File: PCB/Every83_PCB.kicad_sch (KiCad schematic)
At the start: 31 parts, among them J1 781710004, J3 SM03B-SRSS-TB, J4 SM03B-SRSS-TB, Q3 DMG2305, SW101 KMR2, SW102 KMR2, U2 AP2112(3.3V), U3 MCP73831T-2ACI/OT, X3 JSTPH

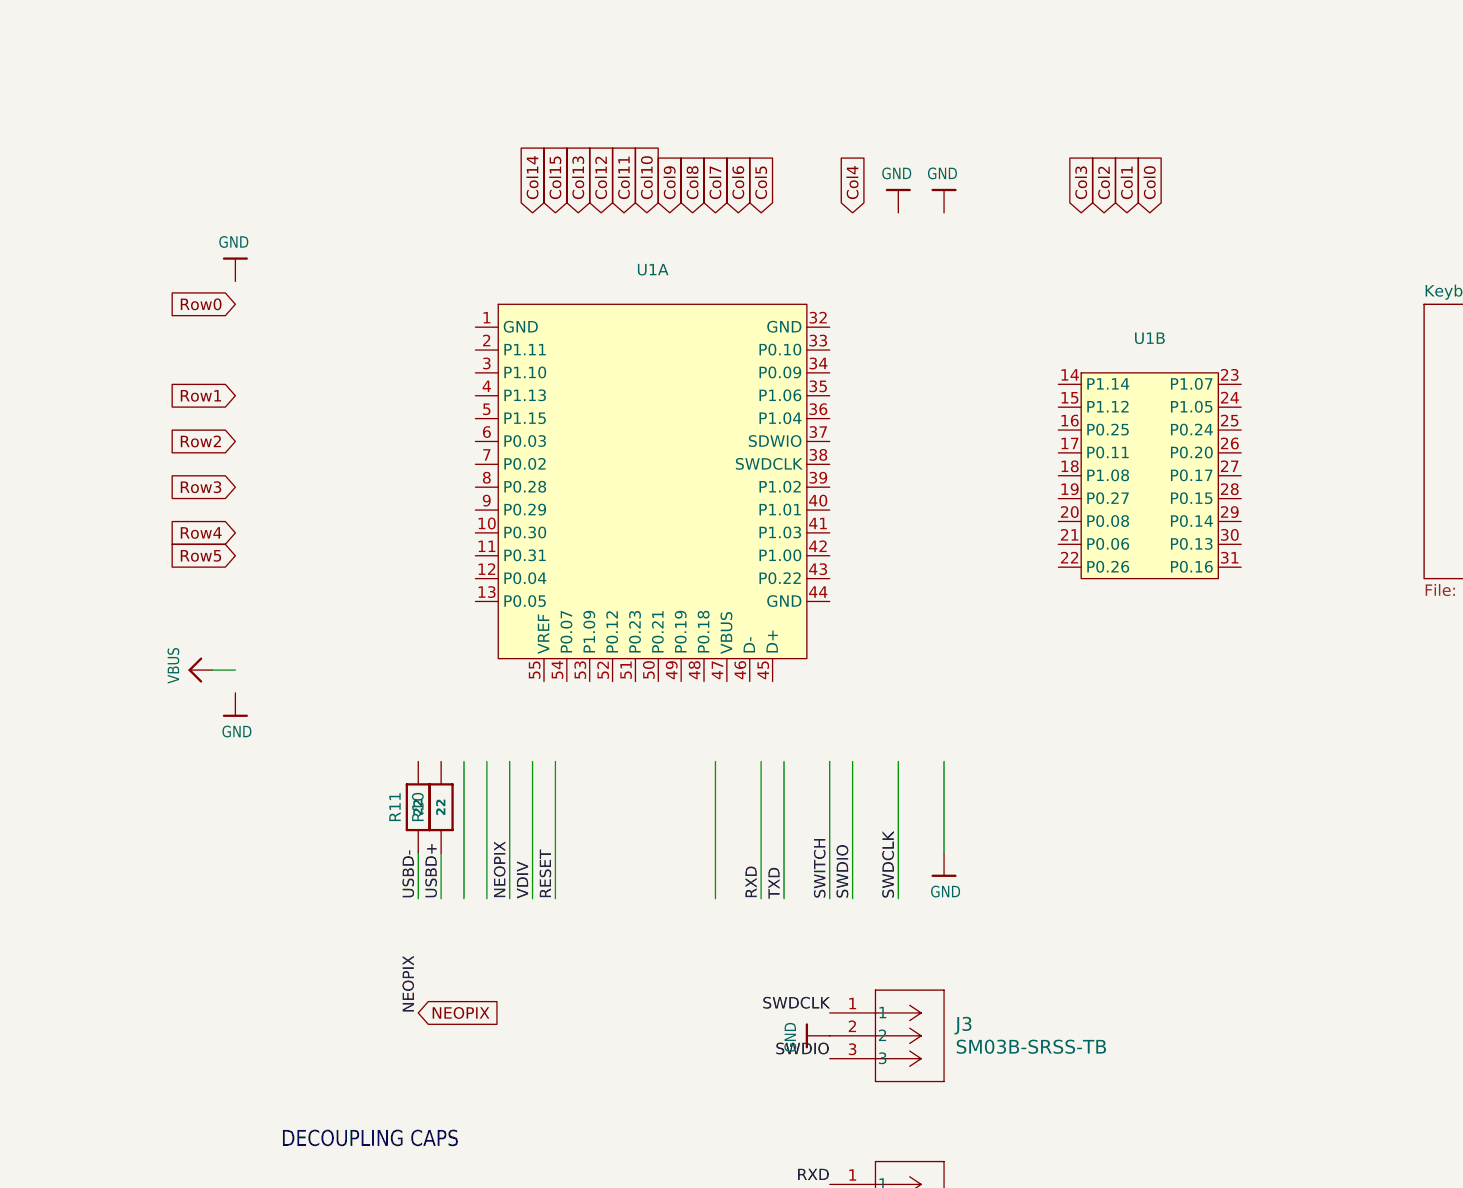
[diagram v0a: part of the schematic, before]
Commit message: Update the microcontroller footprint
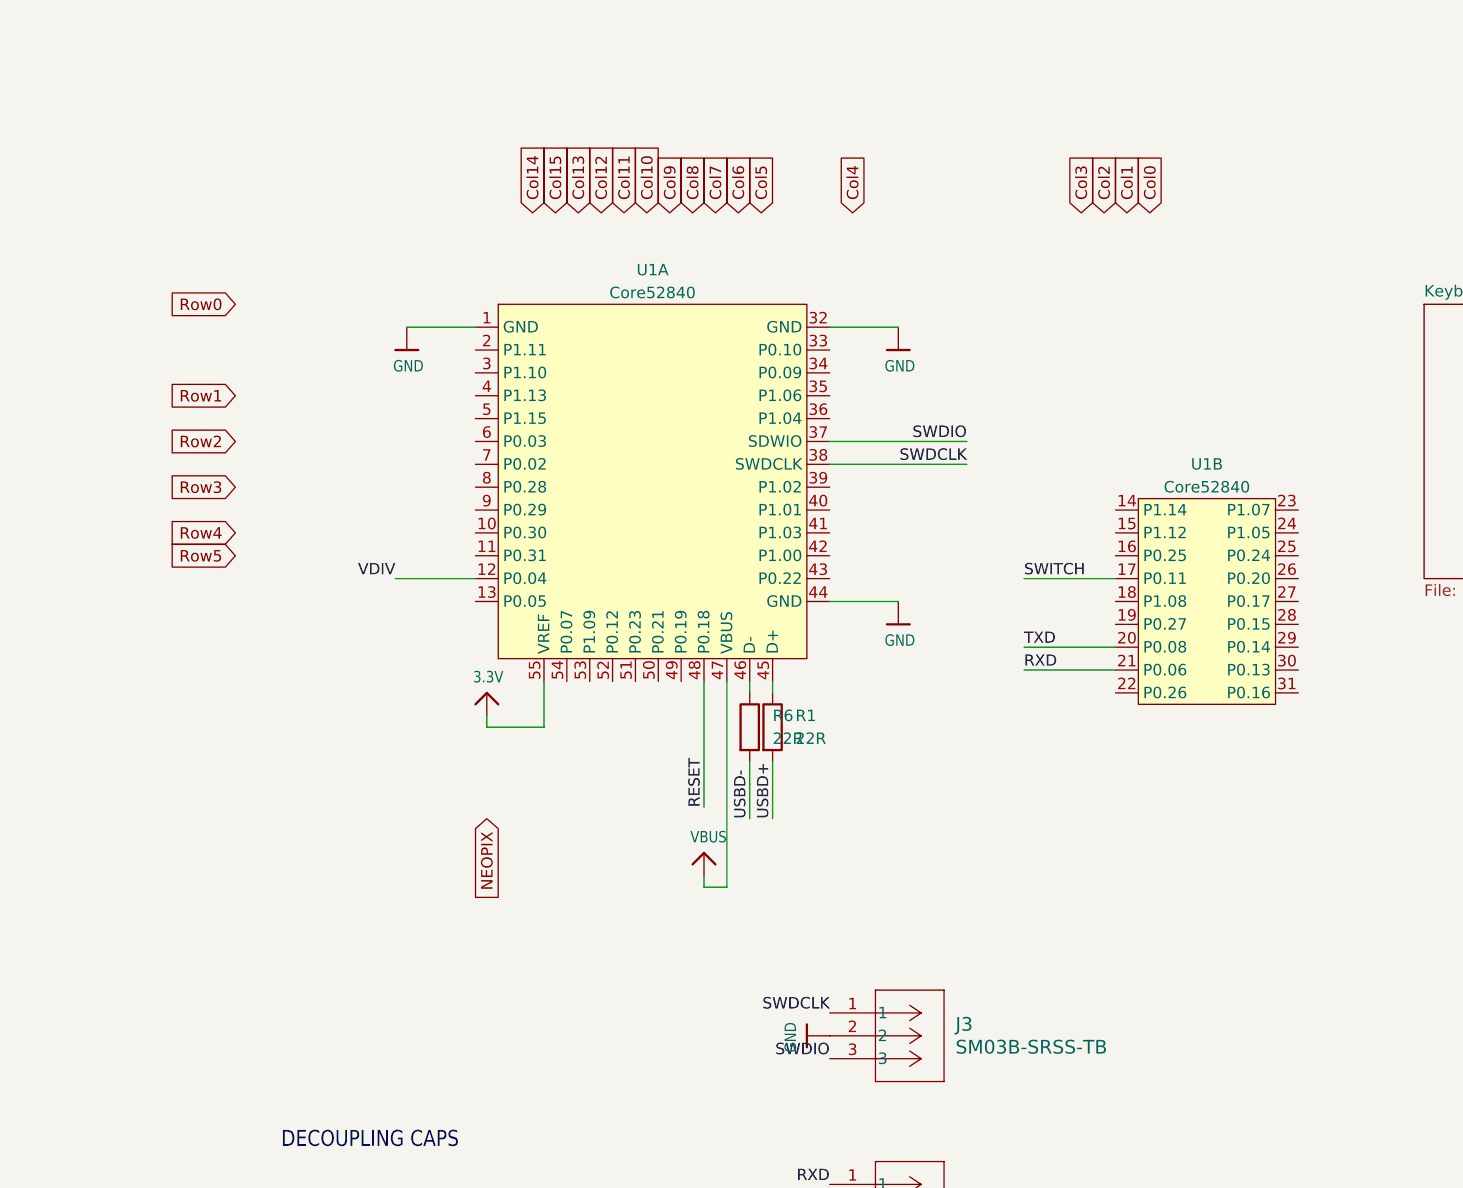
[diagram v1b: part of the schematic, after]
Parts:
- removed R10, R11: 22, Adafruit nRF52840 Bluefruit Feather Express Rev D:0603-NO, symbol Adafruit nRF52840 Bluefruit Feather Express Rev D-eagle-import:RESISTOR_0603_NO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
- added R1, R6: 22R, Resistor_SMD:R_0603_1608Metric, symbol Device:R
- U1: value ~ -> Core52840; footprint (none) -> footprints:Core52840
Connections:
- net 3.3V: now also U1.55 (VREF)
- net GND: now also U1.1 (GND), U1.32 (GND), U1.44 (GND)
- net RESET: now also U1.48 (P0.18)
- net RXD: now also U1.21 (P0.06)
- net SWDCLK: now also U1.38 (SWDCLK)
- net SWDIO: now also U1.37 (SDWIO)
- net SWITCH: now also U1.17 (P0.11)
- net TXD: now also U1.20 (P0.08)
- net USBD+: now also R1.2
- net USBD-: now also R6.2
- net VBUS: now also U1.47 (VBUS)
- net VDIV: now also U1.12 (P0.04)
- net at U1.45 (D+): now also R1.1
- net at U1.46 (D-): now also R6.1
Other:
- moved on the sheet: U1B

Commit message: More work done
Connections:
- net Col0: now also U1.2 (P1.11)
- net Col1: now also U1.3 (P1.10)
- net Col10: now also U1.13 (P0.05)
- net Col2: now also U1.4 (P1.13)
- net Col3: now also U1.5 (P1.15)
- net Col4: now also U1.6 (P0.03)
- net Col5: now also U1.7 (P0.02)
- net Col6: now also U1.8 (P0.28)
- net Col7: now also U1.9 (P0.29)
- net Col8: now also U1.10 (P0.30)
- net Col9: now also U1.11 (P0.31)
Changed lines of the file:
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@@
 	(wire
 		(pts
-			(xy 120.65 81.28) (xy 128.27 81.28)
+			(xy 116.84 81.28) (xy 128.27 81.28)
 		)
 		(stroke
@@
 	(global_label "Col10"
 		(shape input)
-		(at 147.32 68.58 90)
+		(at 128.27 111.76 180)
 		(fields_autoplaced yes)
 		(effects
@@
 				(size 1.27 1.27)
 			)
-			(justify left)
+			(justify right)
 		)
 		(property "Intersheetrefs" "${INTERSHEET_REFS}"
-			(at 147.32 60.171 90)
+			(at 119.7816 111.76 0)
 			(effects
 				(font
 					(size 1.27 1.27)
 				)
-				(justify left)
+				(justify right)
 				(hide yes)
 			)
@@
 	(global_label "Col8"
 		(shape input)
-		(at 152.4 68.58 90)
+		(at 128.27 104.14 180)
 		(fields_autoplaced yes)
 		(effects
@@
 				(size 1.27 1.27)
 			)
-			(justify left)
+			(justify right)
 		)
 		(property "Intersheetrefs" "${INTERSHEET_REFS}"
-			(at 152.4 61.3011 90)
+			(at 120.9911 104.14 0)
 			(effects
 				(font
 					(size 1.27 1.27)
 				)
-				(justify left)
+				(justify right)
 				(hide yes)
 			)
@@
 	(global_label "Col5"
 		(shape input)
-		(at 160.02 68.58 90)
+		(at 128.27 96.52 180)
 		(fields_autoplaced yes)
 		(effects
@@
 				(size 1.27 1.27)
 			)
-			(justify left)
+			(justify right)
 		)
 		(property "Intersheetrefs" "${INTERSHEET_REFS}"
-			(at 160.02 61.3011 90)
+			(at 120.9911 96.52 0)
 			(effects
 				(font
 					(size 1.27 1.27)
 				)
-				(justify left)
+				(justify right)
 				(hide yes)
 			)
@@
 	(global_label "Col7"
 		(shape input)
-		(at 154.94 68.58 90)
+		(at 128.27 101.6 180)
 		(fields_autoplaced yes)
 		(effects
@@
 				(size 1.27 1.27)
 			)
-			(justify left)
+			(justify right)
 		)
 		(property "Intersheetrefs" "${INTERSHEET_REFS}"
-			(at 154.94 61.3011 90)
+			(at 120.9911 101.6 0)
 			(effects
 				(font
 					(size 1.27 1.27)
 				)
-				(justify left)
+				(justify right)
 				(hide yes)
 			)
@@
 	(global_label "Col9"
 		(shape input)
-		(at 149.86 68.58 90)
+		(at 128.27 106.68 180)
 		(fields_autoplaced yes)
 		(effects
@@
 				(size 1.27 1.27)
 			)
-			(justify left)
+			(justify right)
 		)
 		(property "Intersheetrefs" "${INTERSHEET_REFS}"
-			(at 149.86 61.3805 90)
+			(at 120.9911 106.68 0)
 			(effects
 				(font
 					(size 1.27 1.27)
 				)
-				(justify left)
+				(justify right)
 				(hide yes)
 			)
@@
 	(global_label "Col6"
 		(shape input)
-		(at 157.48 68.58 90)
+		(at 128.27 99.06 180)
 		(fields_autoplaced yes)
 		(effects
@@
 				(size 1.27 1.27)
 			)
-			(justify left)
+			(justify right)
 		)
 		(property "Intersheetrefs" "${INTERSHEET_REFS}"
-			(at 157.48 61.3011 90)
+			(at 120.9911 99.06 0)
 			(effects
 				(font
 					(size 1.27 1.27)
 				)
-				(justify left)
+				(justify right)
 				(hide yes)
 			)
@@
 	(global_label "Col2"
 		(shape input)
-		(at 198.12 68.58 90)
+		(at 128.27 88.9 180)
 		(fields_autoplaced yes)
 		(effects
@@
 				(size 1.27 1.27)
 			)
-			(justify left)
+			(justify right)
 		)
 		(property "Intersheetrefs" "${INTERSHEET_REFS}"
-			(at 198.12 61.3011 90)
+			(at 120.9911 88.9 0)
 			(effects
 				(font
 					(size 1.27 1.27)
 				)
-				(justify left)
+				(justify right)
 				(hide yes)
 			)
@@
 	(global_label "Col3"
 		(shape input)
-		(at 195.58 68.58 90)
+		(at 128.27 91.44 180)
 		(fields_autoplaced yes)
 		(effects
@@
 				(size 1.27 1.27)
 			)
-			(justify left)
+			(justify right)
 		)
 		(property "Intersheetrefs" "${INTERSHEET_REFS}"
-			(at 195.58 61.3011 90)
+			(at 120.9911 91.44 0)
 			(effects
 				(font
 					(size 1.27 1.27)
 				)
-				(justify left)
+				(justify right)
 				(hide yes)
 			)
@@
 	(global_label "Col1"
 		(shape input)
-		(at 200.66 68.58 90)
+		(at 128.27 86.36 180)
 		(fields_autoplaced yes)
 		(effects
@@
 				(size 1.27 1.27)
 			)
-			(justify left)
+			(justify right)
 		)
 		(property "Intersheetrefs" "${INTERSHEET_REFS}"
-			(at 200.66 61.3011 90)
+			(at 120.9911 86.36 0)
 			(effects
 				(font
 					(size 1.27 1.27)
 				)
-				(justify left)
+				(justify right)
 				(hide yes)
 			)
@@
 	(global_label "Col0"
 		(shape input)
-		(at 203.2 68.58 90)
+		(at 128.27 83.82 180)
 		(fields_autoplaced yes)
 		(effects
@@
 				(size 1.27 1.27)
 			)
-			(justify left)
+			(justify right)
 		)
 		(property "Intersheetrefs" "${INTERSHEET_REFS}"
-			(at 203.2 61.3011 90)
+			(at 120.9911 83.82 0)
 			(effects
 				(font
 					(size 1.27 1.27)
 				)
-				(justify left)
+				(justify right)
 				(hide yes)
 			)
@@
 	(global_label "Col4"
 		(shape input)
-		(at 170.18 68.58 90)
+		(at 128.27 93.98 180)
 		(fields_autoplaced yes)
 		(effects
@@
 				(size 1.27 1.27)
 			)
-			(justify left)
+			(justify right)
 		)
 		(property "Intersheetrefs" "${INTERSHEET_REFS}"
-			(at 170.18 61.3011 90)
+			(at 120.9911 93.98 0)
 			(effects
 				(font
 					(size 1.27 1.27)
 				)
-				(justify left)
+				(justify right)
 				(hide yes)
 			)
@@
 	(symbol
 		(lib_id "Adafruit nRF52840 Bluefruit Feather Express Rev D-eagle-import:GND")
-		(at 120.65 83.82 0)
+		(at 116.84 83.82 0)
 		(unit 1)
 		(exclude_from_sim no)
@@
 		(dnp no)
 		(property "Reference" "#U$048"
-			(at 120.65 83.82 0)
+			(at 116.84 83.82 0)
 			(effects
 				(font
@@
 		)
 		(property "Value" "GND"
-			(at 119.126 86.36 0)
+			(at 115.316 86.36 0)
 			(effects
 				(font
@@
 		)
 		(property "Footprint" ""
-			(at 120.65 83.82 0)
+			(at 116.84 83.82 0)
 			(effects
 				(font
@@
 		)
 		(property "Datasheet" ""
-			(at 120.65 83.82 0)
+			(at 116.84 83.82 0)
 			(effects
 				(font
@@
 		)
 		(property "Description" ""
-			(at 120.65 83.82 0)
+			(at 116.84 83.82 0)
 			(effects
 				(font

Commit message: Just need to run DRC now
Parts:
- removed D102: RED, Adafruit nRF52840 Bluefruit Feather Express Rev D:CHIPLED_0805_NOOUTLINE, symbol Adafruit nRF52840 Bluefruit Feather Express Rev D-eagle-import:LED0805_NOOUTLINE
- removed D104: BLUE, Adafruit nRF52840 Bluefruit Feather Express Rev D:CHIPLED_0805_NOOUTLINE, symbol Adafruit nRF52840 Bluefruit Feather Express Rev D-eagle-import:LED0805_NOOUTLINE
- added D84, D85: LED, LED_SMD:LED_0805_2012Metric, symbol Device:LED
- R2, R3, R5: footprint Adafruit nRF52840 Bluefruit Feather Express Rev D:0603-NO -> Resistor_SMD:R_0603_1608Metric
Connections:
- net Col11: now also U1.54 (P0.07)
- net Col12: now also U1.53 (P1.09)
- net Col13: now also U1.52 (P0.12)
- net Col14: now also U1.51 (P0.23)
- net Col15: now also U1.50 (P0.21)
- net GND: now also R2.2
- net LED1: now also U1.43 (P0.22), D84.2 (A); no longer R2.1
- net LED2: now also U1.42 (P1.00), D85.2 (A)
- net NEOPIX: now also U1.49 (P0.19)
- net Row0: now also U1.26 (P0.20)
- net Row1: now also U1.27 (P0.17)
- net Row2: now also U1.28 (P0.15)
- net Row3: now also U1.29 (P0.14)
- net Row4: now also U1.30 (P0.13)
- net Row5: now also U1.31 (P0.16)
- net at R5.1: now also D85.1 (K)
- new net: D84.1 (K), R2.1
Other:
- moved on the sheet: R2

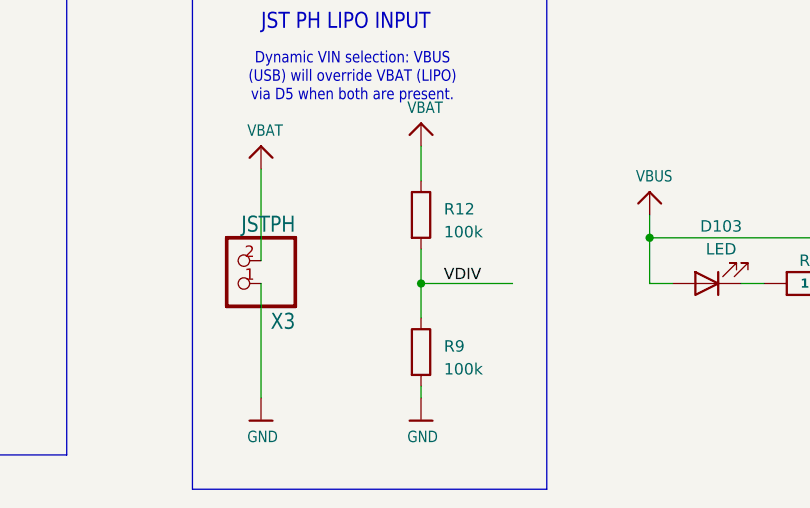
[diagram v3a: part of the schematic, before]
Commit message: change battery connector
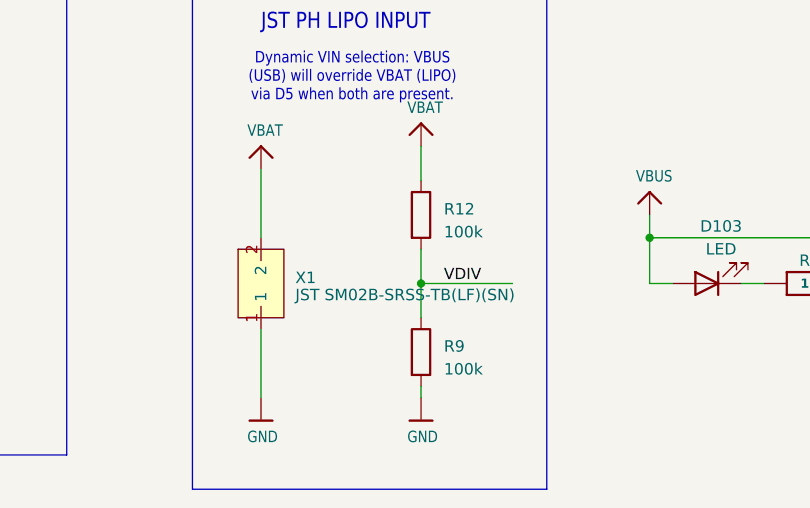
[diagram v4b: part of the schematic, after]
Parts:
- removed X3: JSTPH, Adafruit nRF52840 Bluefruit Feather Express Rev D:JSTPH2, symbol Adafruit nRF52840 Bluefruit Feather Express Rev D-eagle-import:CON_JST_PH_2PIN
- added X1: JST SM02B-SRSS-TB(LF)(SN), Connector_JST:JST_SH_SM02B-SRSS-TB_1x02-1MP_P1.00mm_Horizontal, symbol JohnDeere:SM02B-SRSS-TB
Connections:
- net GND: now also X1.1
- net VBAT: now also X1.2
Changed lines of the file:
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@@
 	(wire
 		(pts
-			(xy 177.8 233.68) (xy 177.8 243.84)
-		)
-		(stroke
-			(width 0.1524)
-			(type solid)
-		)
-	)
-	(wire
-		(pts
 			(xy 121.92 193.04) (xy 121.92 195.58)
 		)
@@
 	(wire
 		(pts
-			(xy 177.8 259.08) (xy 177.8 246.38)
-		)
-		(stroke
-			(width 0.1524)
-			(type solid)
-		)
-	)
-	(wire
-		(pts
 			(xy 153.67 143.51) (xy 156.21 143.51)
 		)
@@
 	(wire
 		(pts
+			(xy 177.8 233.68) (xy 177.8 241.3)
+		)
+		(stroke
+			(width 0)
+			(type default)
+		)
+	)
+	(wire
+		(pts
 			(xy 88.9 254) (xy 88.9 251.46)
 		)
@@
 	(wire
 		(pts
+			(xy 177.8 251.46) (xy 177.8 259.08)
+		)
+		(stroke
+			(width 0)
+			(type default)
+		)
+	)
+	(wire
+		(pts
 			(xy 99.06 243.84) (xy 99.06 238.76)
 		)
@@
 	)
 	(symbol
-		(lib_id "Adafruit nRF52840 Bluefruit Feather Express Rev D-eagle-import:CON_JST_PH_2PIN")
-		(at 175.26 243.84 180)
-		(unit 1)
-		(exclude_from_sim no)
-		(in_bom yes)
-		(on_board yes)
-		(dnp no)
-		(property "Reference" "X3"
-			(at 181.61 249.555 0)
-			(effects
-				(font
-					(size 1.778 1.5113)
-				)
-				(justify left bottom)
-			)
-		)
-		(property "Value" "JSTPH"
-			(at 181.61 238.76 0)
-			(effects
-				(font
-					(size 1.778 1.5113)
-				)
-				(justify left bottom)
-			)
-		)
-		(property "Footprint" "Adafruit nRF52840 Bluefruit Feather Express Rev D:JSTPH2"
-			(at 175.26 243.84 0)
-			(effects
-				(font
-					(size 1.27 1.27)
-				)
-				(hide yes)
-			)
-		)
-		(property "Datasheet" ""
-			(at 175.26 243.84 0)
-			(effects
-				(font
-					(size 1.27 1.27)
-				)
-				(hide yes)
-			)
-		)
-		(property "Description" ""
-			(at 175.26 243.84 0)
-			(effects
-				(font
-					(size 1.27 1.27)
-				)
-				(hide yes)
-			)
-		)
-		(pin "1"
-		)
-		(pin "2"
-		)
-		(instances
-			(project "Every83_PCB"
-				(path "/ea2432c4-eb7a-431a-b465-8c00cfcb4450"
-					(reference "X3")
-					(unit 1)
-				)
-			)
-		)
-	)
-	(symbol
 		(lib_id "Adafruit nRF52840 Bluefruit Feather Express Rev D-eagle-import:RESISTOR_0603_NOOUT")
 		(at 59.69 238.76 0)
@@
 					(unit 1)
 				)
+			)
+		)
+	)
+	(symbol
+		(lib_id "JohnDeere:SM02B-SRSS-TB")
+		(at 177.8 246.38 0)
+		(unit 1)
+		(exclude_from_sim no)
+		(in_bom yes)
+		(on_board yes)
+		(dnp no)
+		(fields_autoplaced yes)
+		(property "Reference" "X1"
+			(at 181.61 245.7449 0)
+			(effects
+				(font
+					(size 1.27 1.27)
+				)
+				(justify left)
+			)
+		)
+		(property "Value" "JST SM02B-SRSS-TB(LF)(SN)"
+			(at 181.61 247.65 0)
+			(effects
+				(font
+					(size 1.27 1.27)
+				)
+				(justify left)
+			)
+		)
+		(property "Footprint" "Connector_JST:JST_SH_SM02B-SRSS-TB_1x02-1MP_P1.00mm_Horizontal"
+			(at 177.8 246.38 0)
+			(effects
+				(font
+					(size 1.27 1.27)
+				)
+				(hide yes)
+			)
+		)
+		(property "Datasheet" ""
+			(at 177.8 246.38 0)
+			(effects
+				(font
+					(size 1.27 1.27)
+				)
+				(hide yes)
+			)
+		)
+		(property "Description" ""
+			(at 177.8 246.38 0)
+			(effects
+				(font
+					(size 1.27 1.27)
+				)
+				(hide yes)
+			)
+		)
+		(pin "1"
+		)
+		(pin "2"
+		)
+		(pin "4"
+		)
+		(pin "3"
+		)
+		(instances
+			(project "Every83_PCB"
+				(path "/ea2432c4-eb7a-431a-b465-8c00cfcb4450"
+					(reference "X1")
+					(unit 1)
+				)

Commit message: add breakout wires
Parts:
- added J2, J5: Conn_01x08_Socket, Connector_PinHeader_2.54mm:PinHeader_1x08_P2.54mm_Vertical, symbol Connector:Conn_01x08_Socket
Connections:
- net 8: now reaches U1.14 (P1.14)
- net 8: now also J2.8 (Pin_8)
- net 9: now reaches U1.15 (P1.12)
- net 9: now also J5.1 (Pin_1)
- net 10: now reaches U1.16 (P0.25)
- net 10: now also J5.2 (Pin_2)
- net 11: now reaches U1.18 (P1.08)
- net 11: now also J5.3 (Pin_3)
- net 12: now reaches U1.19 (P0.27)
- net 12: now also J5.4 (Pin_4)
- net 13: now reaches U1.22 (P0.26)
- net 13: now also J5.5 (Pin_5)
- net 14: now reaches U1.23 (P1.07)
- net 14: now also J5.6 (Pin_6)
- net 15: now reaches U1.24 (P1.05)
- net 15: now also J5.7 (Pin_7)
- net 16: now reaches U1.25 (P0.24)
- net 16: now also J5.8 (Pin_8)
- net 1: now reaches U1.33 (P0.10)
- net 1: now also J2.1 (Pin_1)
- net 2: now reaches U1.34 (P0.09)
- net 2: now also J2.2 (Pin_2)
- net 3: now reaches U1.35 (P1.06)
- net 3: now also J2.3 (Pin_3)
- net 4: now reaches U1.36 (P1.04)
- net 4: now also J2.4 (Pin_4)
- net 5: now reaches U1.39 (P1.02)
- net 5: now also J2.5 (Pin_5)
- net 6: now reaches U1.40 (P1.01)
- net 6: now also J2.6 (Pin_6)
- net 7: now reaches U1.41 (P1.03)
- net 7: now also J2.7 (Pin_7)
